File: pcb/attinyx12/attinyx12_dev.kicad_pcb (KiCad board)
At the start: 2 copper layers, 22.6 x 52 mm, 24 parts, among them J1 USB_C_Receptacle_USB2.0_16P, J2 Conn_01x04, J3 Conn_01x04, J4 Conn_02x06, U1 USBLC6-2SC6, U2 ATtiny212-SS, U3 CH342K

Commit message: final layout
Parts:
- J1: footprint Connector_USB:USB_C_Receptacle_G-Switch_GT-USB-7010ASV -> pl_USB:USB_C_Receptacle_G-Switch_GT-USB-7010ASV
- moved R1 14.8 mm to (74.9, 43.1), turned to 180 degrees
- moved D4 8.87 mm to (88.3, 35.6)
- moved C4 2.98 mm to (85.1, 47.1)
- moved D2 1.81 mm to (75.6, 46.3), turned to 90 degrees
- moved C5 1.80 mm to (79.8, 48.2), turned to 180 degrees
- moved R5 1.52 mm to (86.5, 42.8)
- moved C2 1.22 mm to (74.9, 41.4)
- moved D3 1.00 mm to (85.9, 45.1)
- moved R2 1.00 mm to (85.1, 39.1)
- moved R3 1.00 mm to (85.1, 37.4)
- moved R4 1.00 mm to (85.1, 40.8)
- moved U3 1.00 mm to (80.0, 43.5)
- moved C3 0.91 mm to (75.2, 61.8), turned to -90 degrees
- moved F1 0.84 mm to (74.7, 37.8)
- moved U2 0.60 mm to (80.0, 63.0)
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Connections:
- D1 pad 1: Net-(D1-K) -> GND
- D1 pad 2: VBUS -> Net-(D1-A)
- R1 pad 1: Net-(D1-K) -> VBUS
- R1 pad 2: GND -> Net-(D1-A)
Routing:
- net /LED: track 0.00 -> 22.7 mm
- net /TX: track 0.00 -> 14.5 mm, vias 0 -> 2
- net VBUS: track 4.69 -> 17.3 mm
- net +5V: track 1.97 -> 13.2 mm
- net Net-(D1-A): track 0.00 -> 9.52 mm
- net /RX: track 0.00 -> 8.56 mm, vias 0 -> 2
- net Net-(D4-K): track 0.00 -> 6.38 mm
- net /PA2: track 12.9 -> 15.4 mm
- net Net-(U3-V3): track 1.82 -> 3.19 mm
- net /UD+: track 6.57 -> 5.24 mm
- net Net-(D3-A): track 8.42 -> 7.25 mm
- net /UD-: track 3.64 -> 2.64 mm
- net Net-(J1-CC1): track 11.7 -> 12.7 mm
- net /UPDI: track 17.6 -> 16.6 mm
- net /PA6: track 28.0 -> 27.2 mm
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- added copper zone on F.Cu, net (none)
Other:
- board size 22.6 x 52 mm -> 22.6 x 51 mm

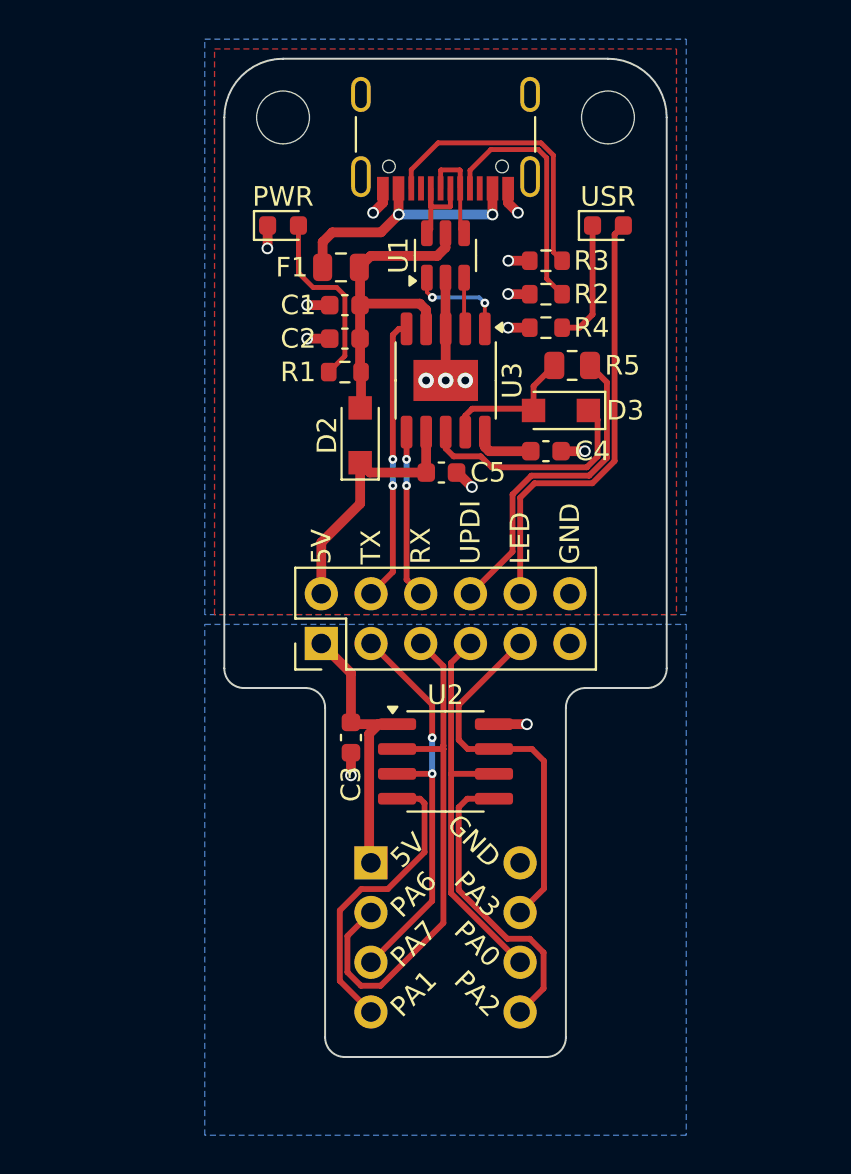
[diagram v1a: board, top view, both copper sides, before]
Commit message: add silkscreen
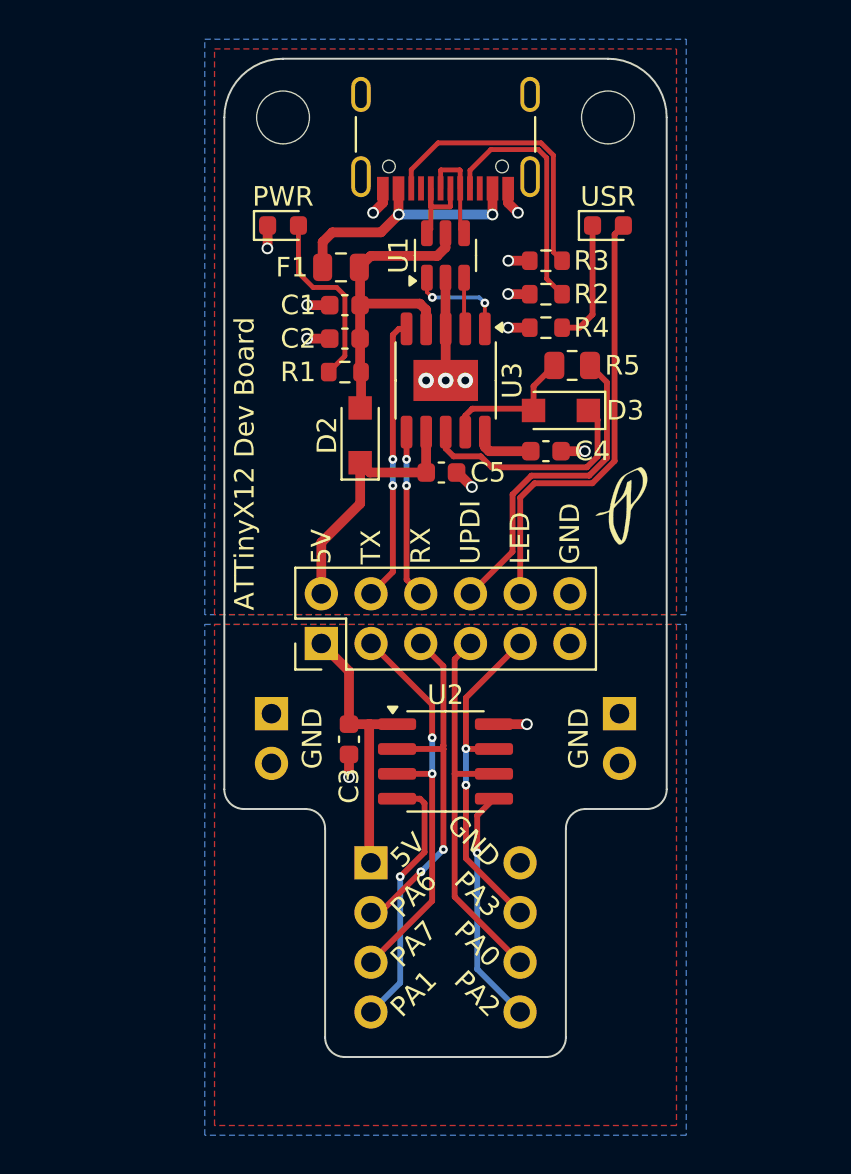
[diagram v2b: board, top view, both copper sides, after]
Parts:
- added G***: LOGO, pl_logo:logo_height_4mm, F.Cu at (89.0, 50.0)
- added J5: Conn_01x02, Connector_PinHeader_2.54mm:PinHeader_1x02_P2.54mm_Vertical, B.Cu at (71.1, 60.6)
- added J6: Conn_01x02, Connector_PinHeader_2.54mm:PinHeader_1x02_P2.54mm_Vertical, B.Cu at (88.9, 60.6)
- added QR*****: https://github.com/sdp8483/attiny_devboard, pl_PCB_artwork:Github QR Code, B.Cu at (80.0, 44.0)
- moved C3 0.13 mm to (75.1, 61.9)
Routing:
- net /PA6: track 27.2 -> 18.4 mm, vias 0 -> 2
- net /PA2: track 15.4 -> 12.2 mm, vias 0 -> 1
- net /PA1: track 15.4 -> 13.3 mm, vias 0 -> 1
- net /PA3: track 19.3 -> 17.5 mm, vias 0 -> 2
- net +5VA: track 15.3 -> 14.3 mm
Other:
- outline, holes or cut-outs redrawn
- board text added: "ATTinyX12 Dev Board"
- board text added: "M2.5"
- board text added: "Sam Perry Feb 2025"
- board text added: "sdp8483/attiny_devboard"
